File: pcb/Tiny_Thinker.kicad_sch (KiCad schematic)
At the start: 43 parts, among them J2 Conn_02x20_Odd_Even, J3 SWD, J4 SPI1, J5 I2C1_A, J6 I2C1_B, J7 Conn_02x20_Odd_Even, J8 USB_C_Receptacle_USB2.0_16P, SW1 SW_Push, SW2 SW_SPDT, U1 STM32F446RET6, U2 AMS1117-3.3, U3 USBLC6-2SC6, Y1 16MHz

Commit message: more comments
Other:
- note added: "+VBUSF from Pi Filter, connected to USB (nom. +5V) 22uF from AMS1117 Datasheet Pg 5"
- note added: "Value specified Datasheet Pg77 Table 18"
- note removed: "Value specified Datasheet Pg77"
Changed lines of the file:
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@@
+		)
+	)
+	(text "+VBUSF from Pi Filter, connected to USB (nom. +5V)\n22uF from AMS1117 Datasheet Pg 5"
+		(exclude_from_sim no)
+		(at 145.542 71.628 0)
+		(effects
+			(font
+				(size 1.27 1.27)
+				(thickness 0.254)
+				(bold yes)
+			)
 		)
 	)
@@
 		)
 	)
-	(text "Value specified Datasheet Pg77\n"
+	(text "Value specified Datasheet Pg77\nTable 18"
 		(exclude_from_sim no)
-		(at 113.538 233.68 0)
+		(at 113.538 234.696 0)
 		(effects
 			(font

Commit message: Assigned footprints
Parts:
- removed J7: Conn_02x20_Odd_Even, Connector_PinHeader_2.54mm:PinHeader_2x20_P2.54mm_Vertical, symbol Connector_Generic:Conn_02x20_Odd_Even
- added J1: Conn_02x20_Odd_Even, Connector_PinHeader_2.54mm:PinHeader_2x20_P2.54mm_Vertical, symbol Connector_Generic:Conn_02x20_Odd_Even
- C16, C17: footprint (none) -> Capacitor_SMD:C_0603_1608Metric
- R5, R6, R7: footprint (none) -> Resistor_SMD:R_0402_1005Metric
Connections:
- net PA1 is gone; now on net GND: J2.8 (Pin_8)
- net PA10 is gone; now on net GND: J2.15 (Pin_15)
- net PA2 is gone; now on net GND: J2.9 (Pin_9)
- net PA9 is gone; now on net GND: J2.14 (Pin_14)
- net PB0 is gone; now on net +3.3V: J2.19 (Pin_19)
- net PB1 is gone; now on net GND: J2.20 (Pin_20)
- net PB12 is gone; now on net GND: J2.32 (Pin_32)
- net PB13 is gone; now on net GND: J2.33 (Pin_33)
- net PB2 is gone; now on net GND: J2.21 (Pin_21)
- net PB3 is gone; now on net +3.3V: J2.22 (Pin_22)
- net PB5 is gone; now on net GND: J2.26 (Pin_26)
- net PB8 is gone; now on net GND: J2.27 (Pin_27)
- net +3.3V: now also J2.1 (Pin_1), J2.37 (Pin_37), J1.1 (Pin_1), J1.19 (Pin_19), J1.22 (Pin_22), J1.37 (Pin_37), J1.4 (Pin_4), J1.40 (Pin_40); no longer J2.3 (Pin_3), J2.39 (Pin_39)
- net GND: now also J2.3 (Pin_3), J2.39 (Pin_39), J1.14 (Pin_14), J1.15 (Pin_15), J1.2 (Pin_2), J1.20 (Pin_20), J1.21 (Pin_21), J1.26 (Pin_26), J1.27 (Pin_27), J1.3 (Pin_3), J1.32 (Pin_32), J1.33 (Pin_33), J1.38 (Pin_38), J1.39 (Pin_39), J1.8 (Pin_8), J1.9 (Pin_9); no longer J2.1 (Pin_1), J2.11 (Pin_11), J2.12 (Pin_12), J2.17 (Pin_17), J2.18 (Pin_18), J2.23 (Pin_23), J2.24 (Pin_24), J2.29 (Pin_29), J2.30 (Pin_30), J2.35 (Pin_35), J2.36 (Pin_36), J2.37 (Pin_37), J2.5 (Pin_5), J2.6 (Pin_6)
- net PA0: no longer names the net of J2.7 (Pin_7)
- net PA15: no longer names the net of J2.16 (Pin_16)
- net PA3: no longer names the net of J2.10 (Pin_10)
- net PA8: no longer names the net of J2.13 (Pin_13)
- net PB10: no longer names the net of J2.31 (Pin_31)
- net PB14: no longer names the net of J2.34 (Pin_34)
- net PB4: no longer names the net of J2.25 (Pin_25)
- net PB9: no longer names the net of J2.28 (Pin_28)
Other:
- moved on the sheet: J2, J3, J4, J5, J6

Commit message: gave colors to all netclasses
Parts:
- renumbered U3 to D1
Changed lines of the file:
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@@
 	)
 	(rectangle
-		(start 168.91 199.39)
-		(end 179.07 204.47)
-		(stroke
-			(width 0)
-			(type default)
-		)
-		(fill
-			(type none)
-		)
-	)
-	(rectangle
 		(start 205.74 21.59)
 		(end 255.905 73.66)
@@
 	)
 	(rectangle
-		(start 168.91 173.99)
-		(end 177.165 179.07)
-		(stroke
-			(width 0)
-			(type default)
-		)
-		(fill
-			(type none)
-		)
-	)
-	(rectangle
-		(start 168.91 140.97)
-		(end 179.07 151.13)
-		(stroke
-			(width 0)
-			(type default)
-		)
-		(fill
-			(type none)
-		)
-	)
-	(rectangle
-		(start 168.91 151.13)
-		(end 179.07 161.29)
-		(stroke
-			(width 0)
-			(type default)
-		)
-		(fill
-			(type none)
-		)
-	)
-	(rectangle
-		(start 168.91 168.91)
-		(end 177.165 173.99)
-		(stroke
-			(width 0)
-			(type default)
-		)
-		(fill
-			(type none)
-		)
-	)
-	(rectangle
 		(start 262.89 21.59)
 		(end 367.538 90.805)
@@
 		)
 	)
-	(rectangle
-		(start 168.91 204.47)
-		(end 177.8 209.55)
-		(stroke
-			(width 0)
-			(type default)
-		)
-		(fill
-			(type none)
-		)
-	)
 	(text "Tiny Thinker STM32 PCB\n"
 		(exclude_from_sim no)
@@
 		(on_board yes)
 		(dnp no)
-		(property "Reference" "U3"
+		(property "Reference" "D1"
 			(at 318.3889 49.53 0)
 			(effects
@@
 			(project ""
 				(path "/1492d82e-cea7-4984-859f-7eb0a1e67ad8"
-					(reference "U3")
+					(reference "D1")
 					(unit 1)
 				)

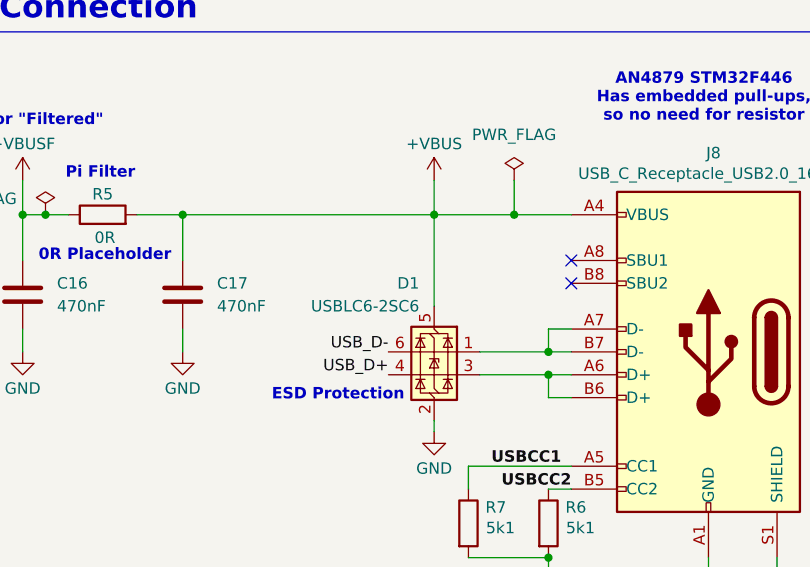
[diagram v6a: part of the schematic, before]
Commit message: Added JLCPCB capabilities
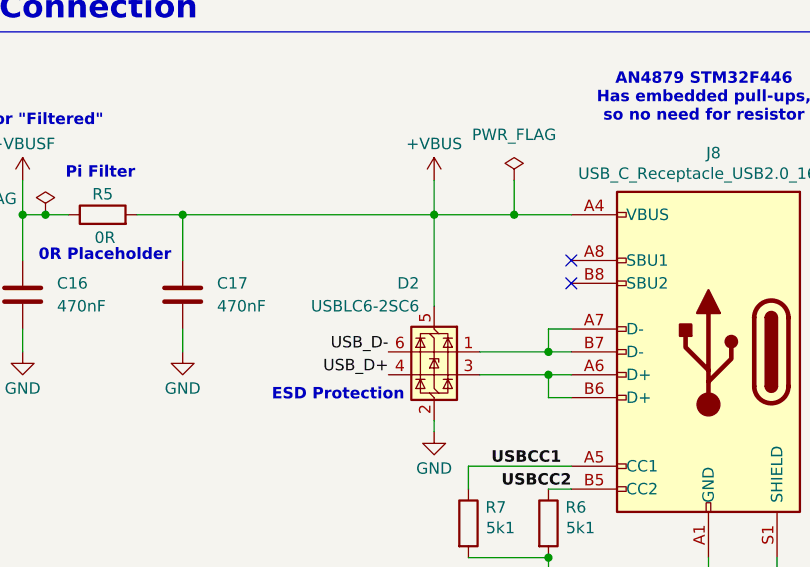
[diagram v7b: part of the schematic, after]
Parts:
- renumbered D1 to D2
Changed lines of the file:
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@@
 		(on_board yes)
 		(dnp no)
-		(property "Reference" "D1"
+		(property "Reference" "D2"
 			(at 318.3889 49.53 0)
 			(effects
@@
 			(project ""
 				(path "/1492d82e-cea7-4984-859f-7eb0a1e67ad8"
-					(reference "D1")
+					(reference "D2")
 					(unit 1)
 				)

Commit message: checkpoint
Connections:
- net TIM3_CH1: now also U1.37 (PC6); no longer U1.56 (PB4)
- net TIM3_CH2: now also U1.38 (PC7); no longer U1.57 (PB5)
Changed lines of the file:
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@@
+	)
+	(no_connect
+		(at 168.91 199.39)
 	)
 	(no_connect
@@
 	)
 	(no_connect
-		(at 128.27 181.61)
-	)
-	(no_connect
 		(at 128.27 204.47)
 	)
@@
 	)
 	(no_connect
-		(at 128.27 184.15)
-	)
-	(no_connect
 		(at 168.91 214.63)
 	)
@@
 		(at 128.27 201.93)
 	)
+	(no_connect
+		(at 168.91 196.85)
+	)
 	(wire
 		(pts
@@
 	)
 	(label "TIM3_CH1"
-		(at 168.91 196.85 0)
+		(at 128.27 181.61 180)
 		(effects
 			(font
 				(size 1.27 1.27)
 			)
-			(justify left bottom)
+			(justify right bottom)
 		)
 	)
@@
 	)
 	(label "TIM3_CH2"
-		(at 168.91 199.39 0)
+		(at 128.27 184.15 180)
 		(effects
 			(font
 				(size 1.27 1.27)
 			)
-			(justify left bottom)
-		)
-	)
+			(justify right bottom)
+		)
+	)
